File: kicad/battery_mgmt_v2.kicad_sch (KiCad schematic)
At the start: 18 parts, among them J301 BATTERY_CONN, Q301 2N7002, U301 BQ21061

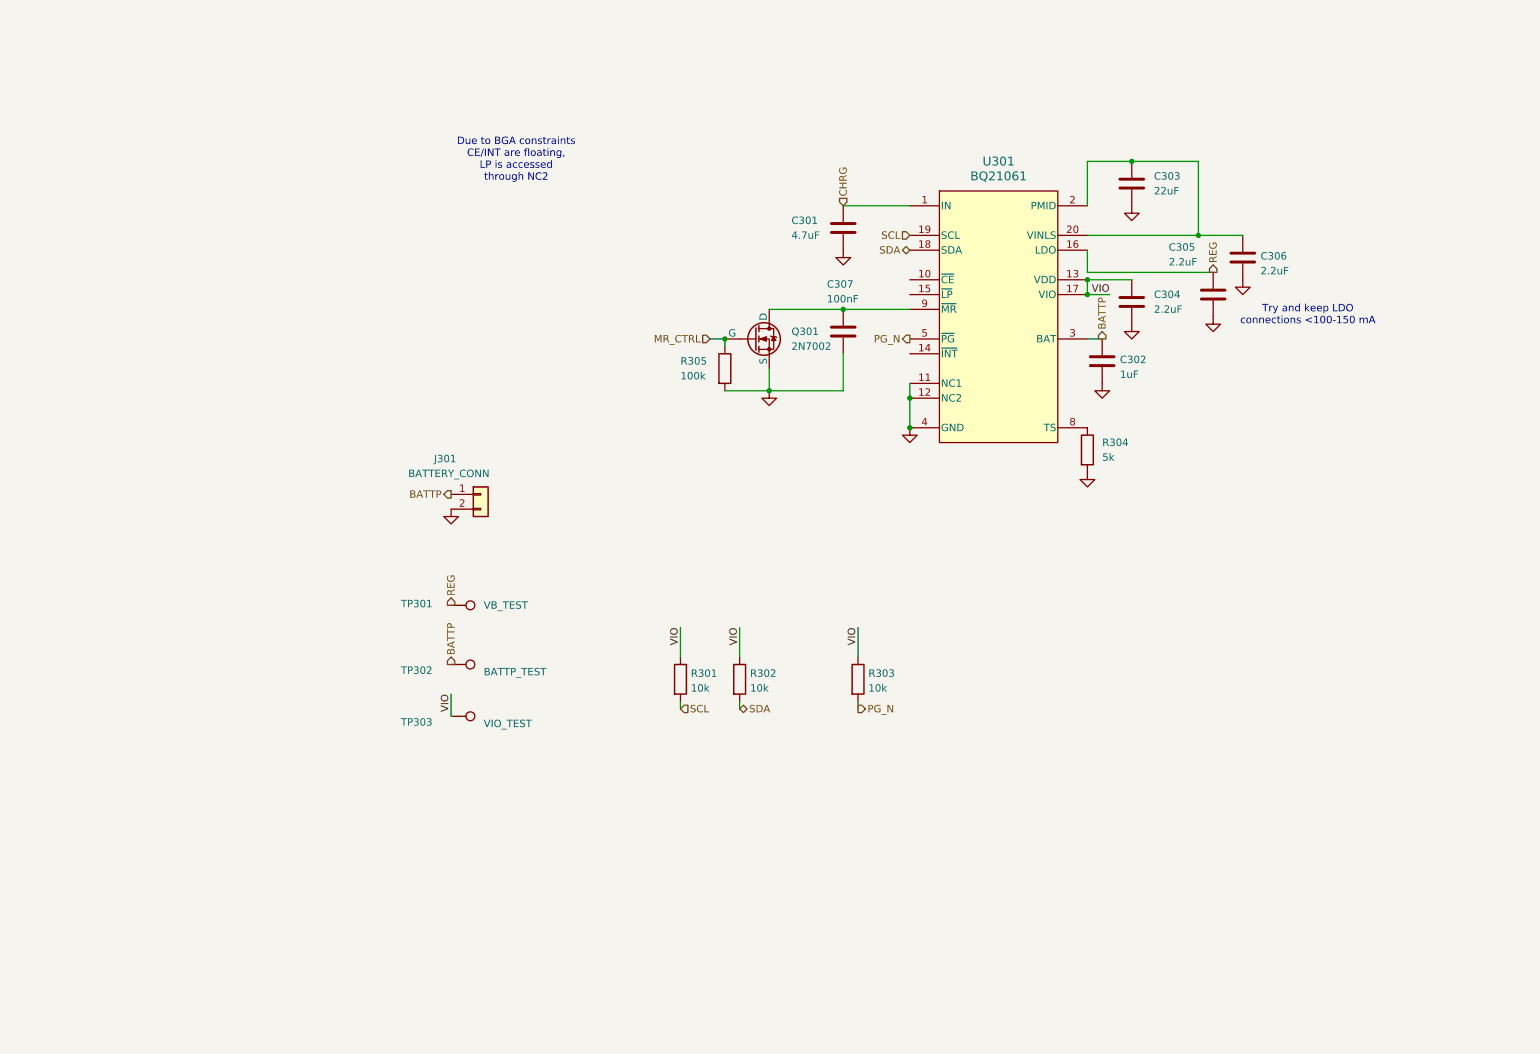
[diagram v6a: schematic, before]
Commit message: add BQ25185 symbol, start battery design with it
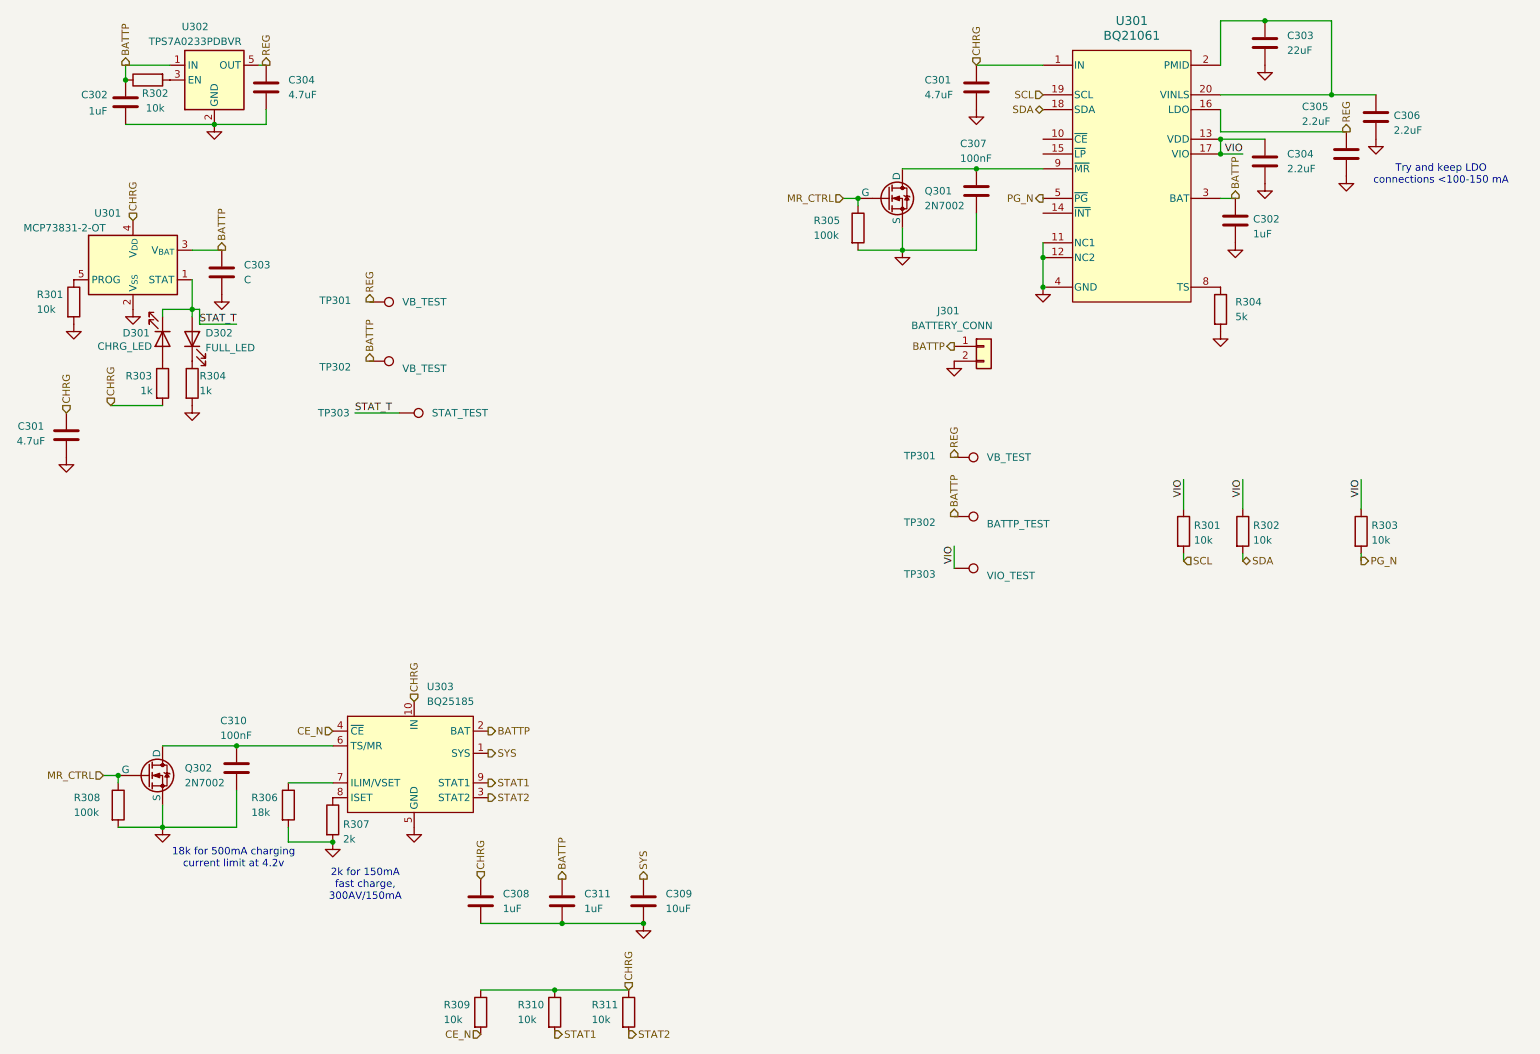
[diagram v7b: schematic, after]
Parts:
- added C301, C304: 4.7uF, symbol Device:C
- added C302, C308, C311: 1uF, symbol Device:C
- added C303: C, symbol Device:C
- added C309: 10uF, symbol Device:C
- added C310: 100nF, Capacitor_SMD:C_0603_1608Metric_Pad1.08x0.95mm_HandSolder, symbol Device:C
- added D301: CHRG_LED, symbol Device:LED
- added D302: FULL_LED, symbol Device:LED
- added Q302: 2N7002, Package_TO_SOT_SMD:SOT-23-3, symbol Simulation_SPICE:NMOS
- added R301, R302, R309, R310, R311: 10k, symbol Device:R
- added R303, R304: 1k, symbol Device:R
- added R306: 18k, symbol Device:R
- added R307: 2k, symbol Device:R
- added R308: 100k, Resistor_SMD:R_0603_1608Metric_Pad0.98x0.95mm_HandSolder, symbol Device:R
- added TP301, TP302: VB_TEST, symbol Connector:TestPoint
- added TP303: STAT_TEST, symbol Connector:TestPoint
- added U301: MCP73831-2-OT, Package_TO_SOT_SMD:SOT-23-5, symbol Battery_Management:MCP73831-2-OT
- added U302: TPS7A0233PDBVR, Package_TO_SOT_SMD:SOT-23-5, symbol Regulator_Linear:TPS7A0508PDBV
- added U303: BQ25185, symbol Raven:BQ25185
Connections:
- net BATTP: now also C302.1, C303.1, C311.1, R302.1, TP302.1, U301.3 (V_{BAT}), U302.1 (IN), U303.2 (BAT)
- net CHRG: now also C301.2, C308.1, R303.2, R309.1, R310.1, R311.1, U301.4 (V_{DD}), U303.10 (IN)
- net GND: now also C301.1, C302.2, C303.2, C304.2, C308.2, C309.2, C310.2, C311.2, Q302.3 (S), R301.2, R304.2, R306.2, R307.2, R308.2, U301.2 (V_{SS}), U302.2 (GND), U303.5 (GND)
- net MR_CTRL: now also Q302.2 (G), R308.1
- net REG: now also C304.1, TP301.1, U302.5 (OUT)
- new net: C310.1, Q302.1 (D), U303.6 (TS/MR)
- new net: R301.1, U301.5 (PROG)
- new net: D301.2 (A), R303.1
- new net: R302.2, U302.3 (EN)
- new net: D302.1 (K), R304.1
- new net: R306.1, U303.7 (ILIM/VSET)
- new net: R307.1, U303.8 (ISET)
- new net CE_N: R309.2, U303.4 (~{CE})
- new net STAT1: R310.2, U303.9 (STAT1)
- new net STAT2: R311.2, U303.3 (STAT2)
- new net STAT_T: D301.1 (K), D302.2 (A), TP303.1, U301.1 (STAT)
- new net SYS: C309.1, U303.1 (SYS)
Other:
- note added: "18k for 500mA charging current limit at 4.2v"
- note added: "2k for 150mA fast charge, 300AV/150mA"
- note removed: "Due to BGA constraints CE/INT are floating, LP is accessed through NC2"
- moved on the sheet: C301, C302, C303, C304, C305, C306, C307, J301, Q301, R301, R302, R303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

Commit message: new battery management w/ separate LDO/charger almost done
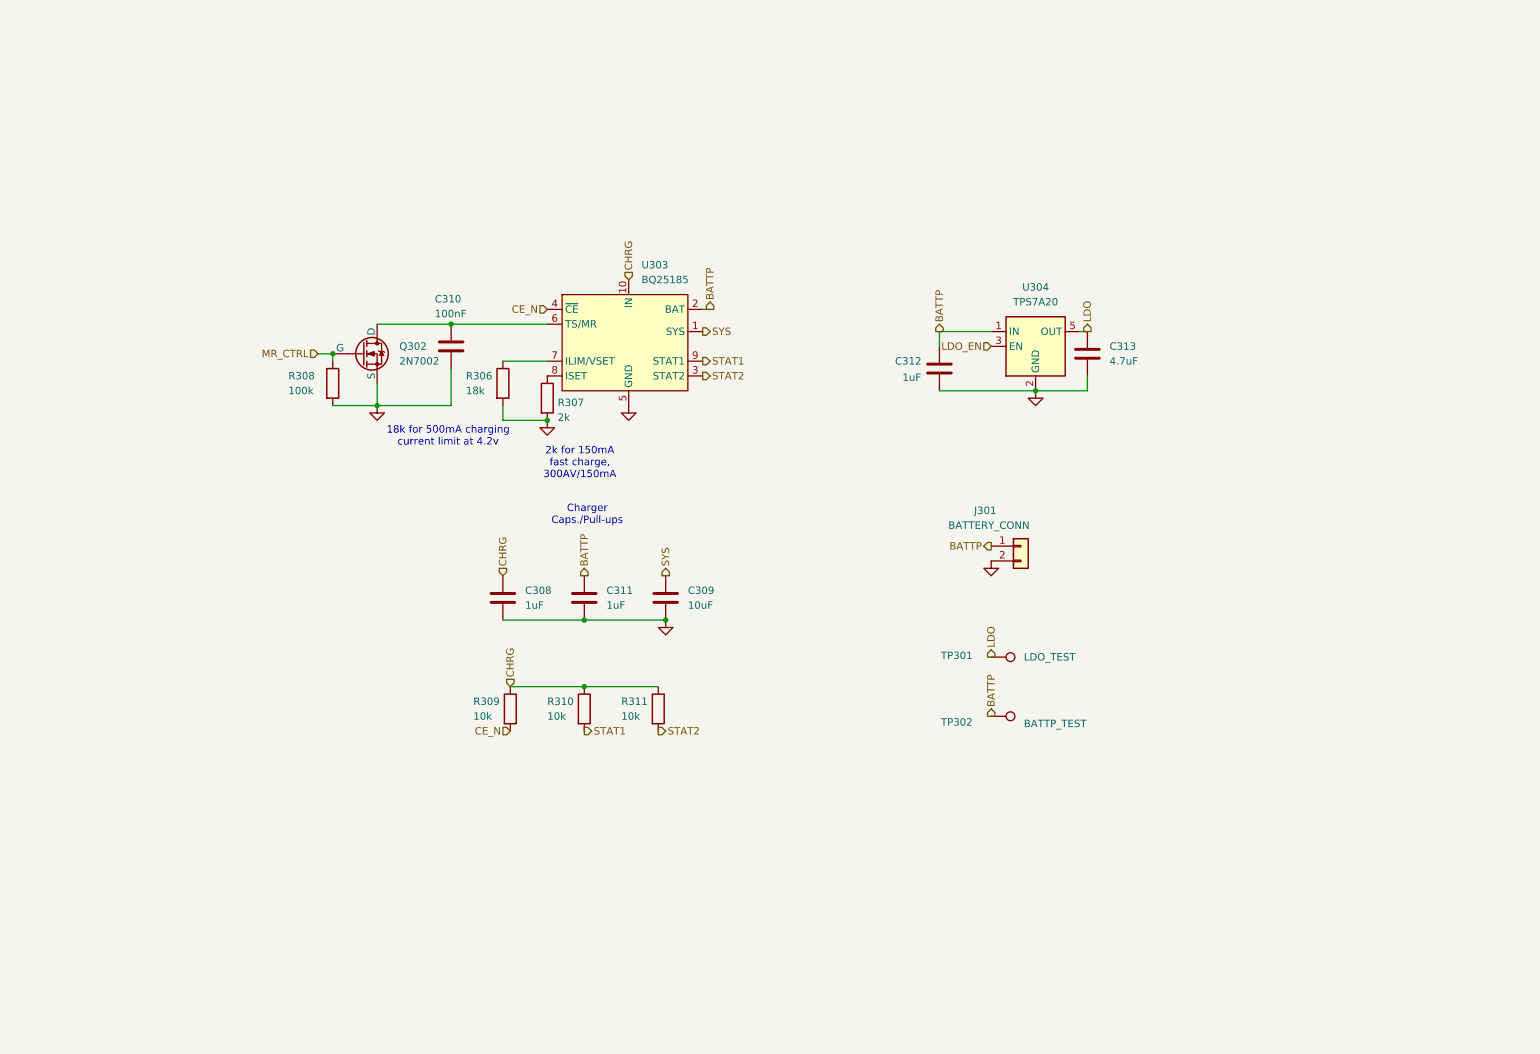
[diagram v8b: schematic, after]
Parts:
- removed C301: 4.7uF, Capacitor_SMD:C_0805_2012Metric_Pad1.18x1.45mm_HandSolder, symbol Device:C
- removed C301, C304: 4.7uF, symbol Device:C
- removed C302: 1uF, symbol Device:C
- removed C302: 1uF, Capacitor_SMD:C_0805_2012Metric_Pad1.18x1.45mm_HandSolder, symbol Device:C
- removed C303: C, symbol Device:C
- removed C303: 22uF, Capacitor_SMD:C_0805_2012Metric_Pad1.18x1.45mm_HandSolder, symbol Device:C
- removed C304, C305, C306: 2.2uF, Capacitor_SMD:C_0603_1608Metric_Pad1.08x0.95mm_HandSolder, symbol Device:C
- removed C307: 100nF, Capacitor_SMD:C_0603_1608Metric_Pad1.08x0.95mm_HandSolder, symbol Device:C
- removed D301: CHRG_LED, symbol Device:LED
- removed D302: FULL_LED, symbol Device:LED
- removed Q301: 2N7002, Package_TO_SOT_SMD:SOT-23-3, symbol Simulation_SPICE:NMOS
- removed R301, R302: 10k, symbol Device:R
- removed R301, R302, R303: 10k, Resistor_SMD:R_0603_1608Metric_Pad0.98x0.95mm_HandSolder, symbol Device:R
- removed R303, R304: 1k, symbol Device:R
- removed R304: 5k, Resistor_SMD:R_0603_1608Metric_Pad0.98x0.95mm_HandSolder, symbol Device:R
- removed R305: 100k, Resistor_SMD:R_0603_1608Metric_Pad0.98x0.95mm_HandSolder, symbol Device:R
- removed TP301, TP302: VB_TEST, symbol Connector:TestPoint
- removed TP303: STAT_TEST, symbol Connector:TestPoint
- removed TP303: VIO_TEST, TestPoint:TestPoint_Pad_D1.5mm, symbol Connector:TestPoint
- removed U301: BQ21061, Raven:WSON10_DLH_TEX-M, symbol Raven:BQ21061
- removed U301: MCP73831-2-OT, Package_TO_SOT_SMD:SOT-23-5, symbol Battery_Management:MCP73831-2-OT
- removed U302: TPS7A0233PDBVR, Package_TO_SOT_SMD:SOT-23-5, symbol Regulator_Linear:TPS7A0508PDBV
- added C312: 1uF, symbol Device:C
- added C313: 4.7uF, symbol Device:C
- added U304: TPS7A20, Package_TO_SOT_SMD:SOT-23-5, symbol Raven:TPS7A20
- TP301: value VB_TEST -> LDO_TEST
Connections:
- net BATTP: now also C312.1, U304.1 (IN)
- net GND: now also C312.2, C313.2, U304.2 (GND)
- net REG renamed LDO
- net LDO: now also C313.1, U304.5 (OUT)
- new net LDO_EN: U304.3 (EN)
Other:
- note added: "Charger Caps./Pull-ups"
- note removed: "Try and keep LDO connections <100-150 mA"
- company: Author: Lucas Merritt -> Mosaic Labs
- title: Battery Management Module V2 -> Battery Management Module
- moved on the sheet: C308, C309, C310, C311, J301, Q302, R306, R307, R308, R309, R310, R311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
